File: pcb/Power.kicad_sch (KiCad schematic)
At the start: 13 parts, among them U4 LD39050PU33R, U5 TLV61048, U6 LDK320AM120R

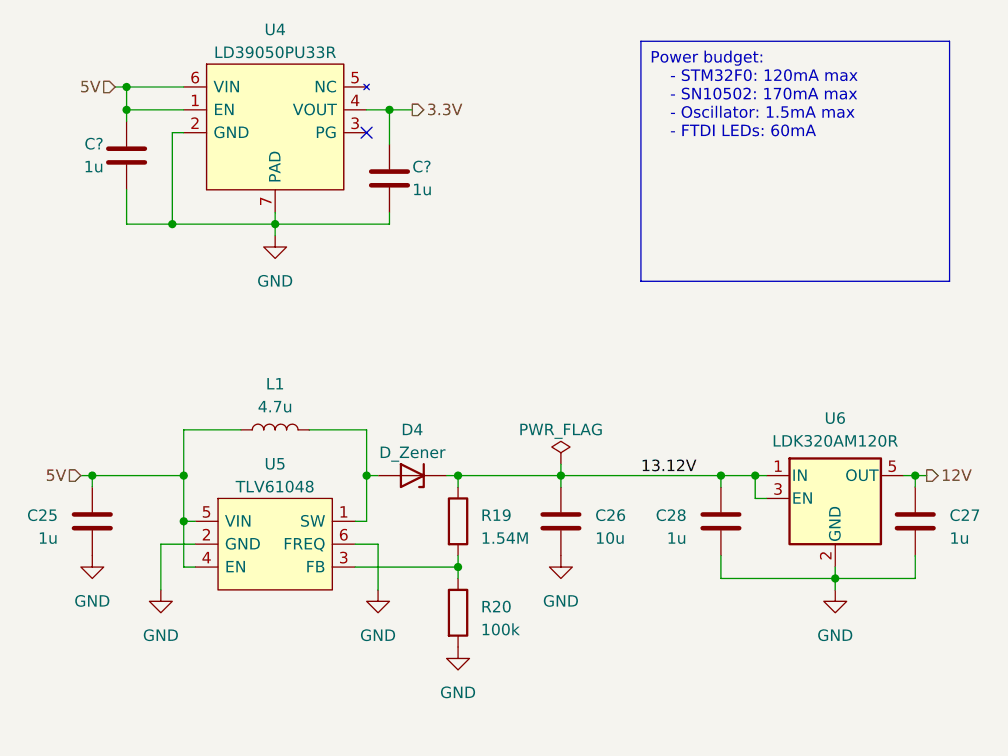
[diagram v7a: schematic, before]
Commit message: Switch to stm32f205
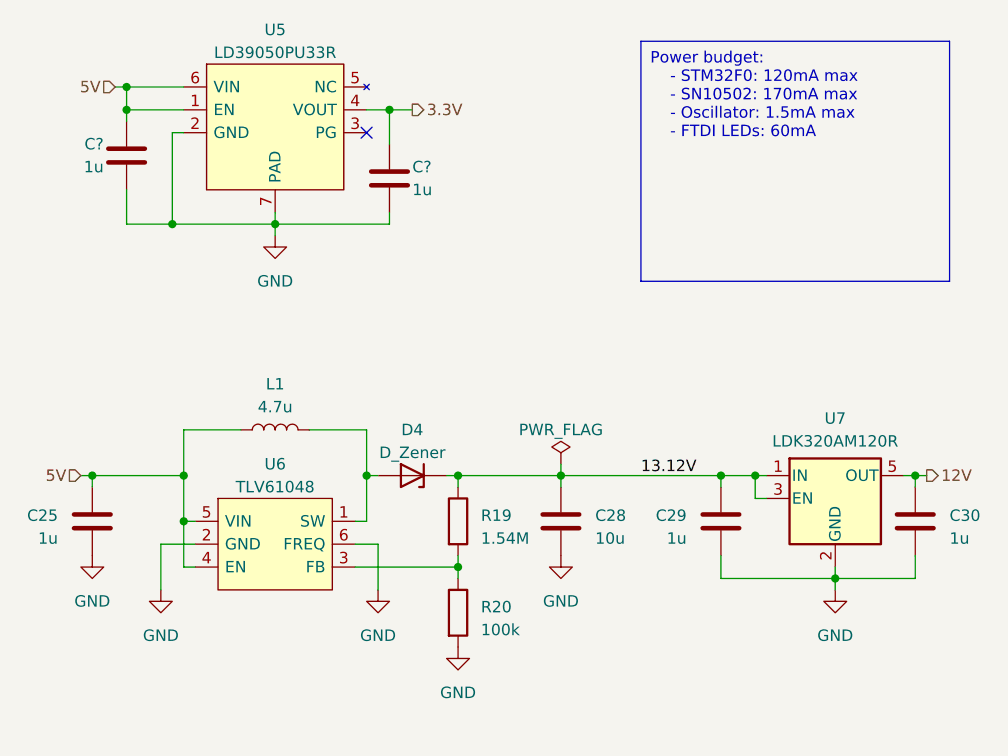
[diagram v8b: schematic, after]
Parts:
- renumbered C26 to C28, C28 to C29, C27 to C30, U4 to U5, U5 to U6, U6 to U7
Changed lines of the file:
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@@
   (symbol (lib_id "Signal Generator Components:LD39050PU33R") (at 110.49 73.66 0) (unit 1)
     (in_bom yes) (on_board yes) (dnp no) (fields_autoplaced)
-    (property "Reference" "U4" (at 123.19 67.31 0)
+    (property "Reference" "U5" (at 123.19 67.31 0)
       (effects (font (size 1.27 1.27)))
     )
@@
       (project "Signal Generator"
         (path "/f6255c48-6253-4c69-a6db-1ceaf4eff04d/755a5482-c972-48ba-877b-a349f74d45fc"
-          (reference "U4") (unit 1)
+          (reference "U5") (unit 1)
         )
       )
@@
   (symbol (lib_id "Signal Generator Components:LDK320AM120R") (at 185.42 119.38 0) (unit 1)
     (in_bom yes) (on_board yes) (dnp no) (fields_autoplaced)
-    (property "Reference" "U6" (at 185.42 110.49 0)
+    (property "Reference" "U7" (at 185.42 110.49 0)
       (effects (font (size 1.27 1.27)))
     )
@@
       (project "Signal Generator"
         (path "/f6255c48-6253-4c69-a6db-1ceaf4eff04d/755a5482-c972-48ba-877b-a349f74d45fc"
-          (reference "U6") (unit 1)
+          (reference "U7") (unit 1)
         )
       )
@@
   (symbol (lib_id "power:PWR_FLAG") (at 154.94 115.57 0) (unit 1)
     (in_bom yes) (on_board yes) (dnp no) (fields_autoplaced)
-    (property "Reference" "#FLG01" (at 154.94 113.665 0)
+    (property "Reference" "#FLG03" (at 154.94 113.665 0)
       (effects (font (size 1.27 1.27)) hide)
     )
@@
       (project "Signal Generator"
         (path "/f6255c48-6253-4c69-a6db-1ceaf4eff04d/755a5482-c972-48ba-877b-a349f74d45fc"
-          (reference "#FLG01") (unit 1)
+          (reference "#FLG03") (unit 1)
         )
       )
@@
         )
         (path "/f6255c48-6253-4c69-a6db-1ceaf4eff04d/755a5482-c972-48ba-877b-a349f74d45fc"
-          (reference "C24") (unit 1)
+          (reference "C27") (unit 1)
         )
       )
@@
   (symbol (lib_id "power:GND") (at 134.62 129.54 0) (unit 1)
     (in_bom yes) (on_board yes) (dnp no) (fields_autoplaced)
-    (property "Reference" "#PWR09" (at 134.62 135.89 0)
+    (property "Reference" "#PWR047" (at 134.62 135.89 0)
       (effects (font (size 1.27 1.27)) hide)
     )
@@
       (project "Signal Generator"
         (path "/f6255c48-6253-4c69-a6db-1ceaf4eff04d/755a5482-c972-48ba-877b-a349f74d45fc"
-          (reference "#PWR09") (unit 1)
+          (reference "#PWR047") (unit 1)
         )
       )
@@
   (symbol (lib_id "Device:C") (at 194.31 121.92 0) (unit 1)
     (in_bom yes) (on_board yes) (dnp no) (fields_autoplaced)
-    (property "Reference" "C27" (at 198.12 121.285 0)
+    (property "Reference" "C30" (at 198.12 121.285 0)
       (effects (font (size 1.27 1.27)) (justify left))
     )
@@
       (project "Signal Generator"
         (path "/f6255c48-6253-4c69-a6db-1ceaf4eff04d/755a5482-c972-48ba-877b-a349f74d45fc"
-          (reference "C27") (unit 1)
+          (reference "C30") (unit 1)
         )
       )
@@
   (symbol (lib_id "Device:C") (at 154.94 121.92 0) (unit 1)
     (in_bom yes) (on_board yes) (dnp no) (fields_autoplaced)
-    (property "Reference" "C26" (at 158.75 121.285 0)
+    (property "Reference" "C28" (at 158.75 121.285 0)
       (effects (font (size 1.27 1.27)) (justify left))
     )
@@
       (project "Signal Generator"
         (path "/f6255c48-6253-4c69-a6db-1ceaf4eff04d/755a5482-c972-48ba-877b-a349f74d45fc"
-          (reference "C26") (unit 1)
+          (reference "C28") (unit 1)
         )
       )
@@
         )
         (path "/f6255c48-6253-4c69-a6db-1ceaf4eff04d/755a5482-c972-48ba-877b-a349f74d45fc"
-          (reference "#PWR0133") (unit 1)
+          (reference "#PWR046") (unit 1)
         )
       )
@@
   (symbol (lib_id "Device:C") (at 172.72 121.92 0) (mirror y) (unit 1)
     (in_bom yes) (on_board yes) (dnp no)
-    (property "Reference" "C28" (at 168.91 121.285 0)
+    (property "Reference" "C29" (at 168.91 121.285 0)
       (effects (font (size 1.27 1.27)) (justify left))
     )
@@
       (project "Signal Generator"
         (path "/f6255c48-6253-4c69-a6db-1ceaf4eff04d/755a5482-c972-48ba-877b-a349f74d45fc"
-          (reference "C28") (unit 1)
+          (reference "C29") (unit 1)
         )
       )
@@
   (symbol (lib_id "power:GND") (at 110.49 129.54 0) (unit 1)
     (in_bom yes) (on_board yes) (dnp no) (fields_autoplaced)
-    (property "Reference" "#PWR05" (at 110.49 135.89 0)
+    (property "Reference" "#PWR045" (at 110.49 135.89 0)
       (effects (font (size 1.27 1.27)) hide)
     )
@@
       (project "Signal Generator"
         (path "/f6255c48-6253-4c69-a6db-1ceaf4eff04d/755a5482-c972-48ba-877b-a349f74d45fc"
-          (reference "#PWR05") (unit 1)
+          (reference "#PWR045") (unit 1)
         )
       )
@@
   (symbol (lib_id "Signal Generator Components:TLV61048") (at 116.84 119.38 0) (unit 1)
     (in_bom yes) (on_board yes) (dnp no) (fields_autoplaced)
-    (property "Reference" "U5" (at 123.19 115.57 0)
+    (property "Reference" "U6" (at 123.19 115.57 0)
       (effects (font (size 1.27 1.27)))
     )
@@
       (project "Signal Generator"
         (path "/f6255c48-6253-4c69-a6db-1ceaf4eff04d/755a5482-c972-48ba-877b-a349f74d45fc"
-          (reference "U5") (unit 1)
+          (reference "U6") (unit 1)
         )
       )
@@
         )
         (path "/f6255c48-6253-4c69-a6db-1ceaf4eff04d/755a5482-c972-48ba-877b-a349f74d45fc"
-          (reference "C23") (unit 1)
+          (reference "C26") (unit 1)
         )
       )
@@
   (symbol (lib_id "power:GND") (at 154.94 125.73 0) (unit 1)
     (in_bom yes) (on_board yes) (dnp no) (fields_autoplaced)
-    (property "Reference" "#PWR03" (at 154.94 132.08 0)
+    (property "Reference" "#PWR049" (at 154.94 132.08 0)
       (effects (font (size 1.27 1.27)) hide)
     )
@@
       (project "Signal Generator"
         (path "/f6255c48-6253-4c69-a6db-1ceaf4eff04d/755a5482-c972-48ba-877b-a349f74d45fc"
-          (reference "#PWR03") (unit 1)
+          (reference "#PWR049") (unit 1)
         )
       )
@@
   (symbol (lib_id "power:GND") (at 185.42 129.54 0) (unit 1)
     (in_bom yes) (on_board yes) (dnp no) (fields_autoplaced)
-    (property "Reference" "#PWR010" (at 185.42 135.89 0)
+    (property "Reference" "#PWR050" (at 185.42 135.89 0)
       (effects (font (size 1.27 1.27)) hide)
     )
@@
       (project "Signal Generator"
         (path "/f6255c48-6253-4c69-a6db-1ceaf4eff04d/755a5482-c972-48ba-877b-a349f74d45fc"
-          (reference "#PWR010") (unit 1)
+          (reference "#PWR050") (unit 1)
         )
       )
@@
   (symbol (lib_id "power:GND") (at 102.87 125.73 0) (unit 1)
     (in_bom yes) (on_board yes) (dnp no) (fields_autoplaced)
-    (property "Reference" "#PWR04" (at 102.87 132.08 0)
+    (property "Reference" "#PWR044" (at 102.87 132.08 0)
       (effects (font (size 1.27 1.27)) hide)
     )
@@
       (project "Signal Generator"
         (path "/f6255c48-6253-4c69-a6db-1ceaf4eff04d/755a5482-c972-48ba-877b-a349f74d45fc"
-          (reference "#PWR04") (unit 1)
+          (reference "#PWR044") (unit 1)
         )
       )
@@
   (symbol (lib_id "power:GND") (at 143.51 135.89 0) (unit 1)
     (in_bom yes) (on_board yes) (dnp no) (fields_autoplaced)
-    (property "Reference" "#PWR02" (at 143.51 142.24 0)
+    (property "Reference" "#PWR048" (at 143.51 142.24 0)
       (effects (font (size 1.27 1.27)) hide)
     )
@@
       (project "Signal Generator"
         (path "/f6255c48-6253-4c69-a6db-1ceaf4eff04d/755a5482-c972-48ba-877b-a349f74d45fc"
-          (reference "#PWR02") (unit 1)
-        )
-      )
+          (reference "#PWR048") (unit 1)
+        )
+      )
